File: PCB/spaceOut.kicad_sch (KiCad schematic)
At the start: 9 parts, among them SW1 SW_Push, SW2 SW_Push, SW3 SW_Push, SW4 SW_Push, SW5 SW_Push, SW6 SW_Push, U1 MOUDLE-SEEEDUINO-XIAO

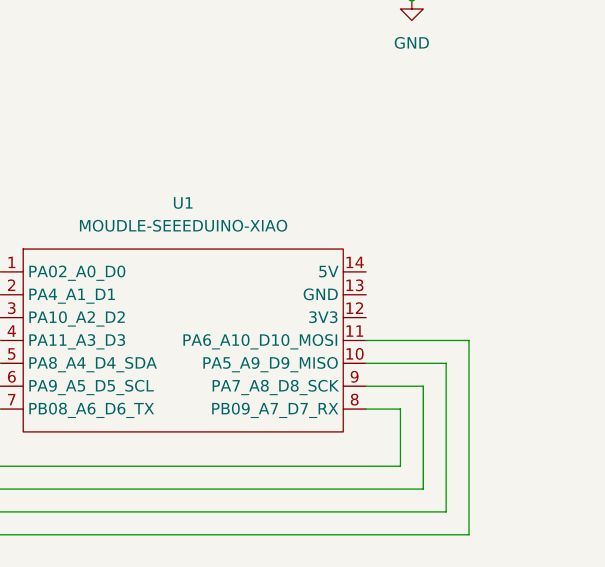
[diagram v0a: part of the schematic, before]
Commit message: added global GND and 5V on XIAO
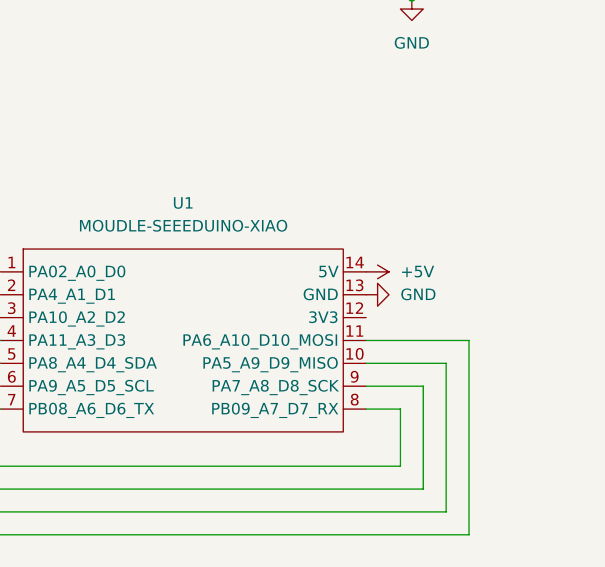
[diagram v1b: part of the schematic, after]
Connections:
- net +5V: now also U1.14 (5V)
- net GND: now also U1.13 (GND)
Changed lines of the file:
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@@
+    )
+  )
+  (symbol (lib_id "power:GND") (at 127 93.98 90) (unit 1)
+    (in_bom yes) (on_board yes) (dnp no) (fields_autoplaced)
+    (property "Reference" "#PWR05" (at 133.35 93.98 0)
+      (effects (font (size 1.27 1.27)) hide)
+    )
+    (property "Value" "GND" (at 130.81 93.98 90)
+      (effects (font (size 1.27 1.27)) (justify right))
+    )
+    (property "Footprint" "" (at 127 93.98 0)
+      (effects (font (size 1.27 1.27)) hide)
+    )
+    (property "Datasheet" "" (at 127 93.98 0)
+      (effects (font (size 1.27 1.27)) hide)
+    )
+    (pin "1")
+    (instances
+      (project "spaceOut"
+        (path "/07b4d0b3-01d1-41ca-826c-c5c9a90b14e2"
+          (reference "#PWR05") (unit 1)
+        )
+      )
     )
   )
@@
         )
       )
+    )
+  )
+  (symbol (lib_id "power:+5V") (at 127 91.44 270) (unit 1)
+    (in_bom yes) (on_board yes) (dnp no) (fields_autoplaced)
+    (property "Reference" "#PWR04" (at 123.19 91.44 0)
+      (effects (font (size 1.27 1.27)) hide)
+    )
+    (property "Value" "+5V" (at 130.81 91.44 90)
+      (effects (font (size 1.27 1.27)) (justify left))
+    )
+    (property "Footprint" "" (at 127 91.44 0)
+      (effects (font (size 1.27 1.27)) hide)
+    )
+    (property "Datasheet" "" (at 127 91.44 0)
+      (effects (font (size 1.27 1.27)) hide)
+    )
+    (pin "1")
+    (instances
+      (project "spaceOut"
+        (path "/07b4d0b3-01d1-41ca-826c-c5c9a90b14e2"
+          (reference "#PWR04") (unit 1)
+        )
+      )
